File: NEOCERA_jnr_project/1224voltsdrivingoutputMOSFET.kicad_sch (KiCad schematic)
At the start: 15 parts, among them Q1 BSS138, Q2 Q_PMOS_GSD, Q3 BSS138, Q4 Q_PMOS_GSD, Q5 BSS138, Q6 Q_PMOS_GSD

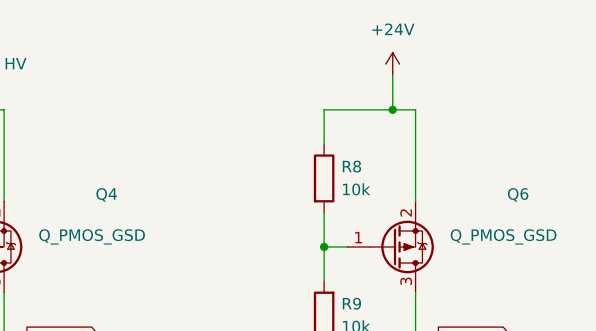
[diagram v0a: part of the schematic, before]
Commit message: changes
edited symbols and usb schematic
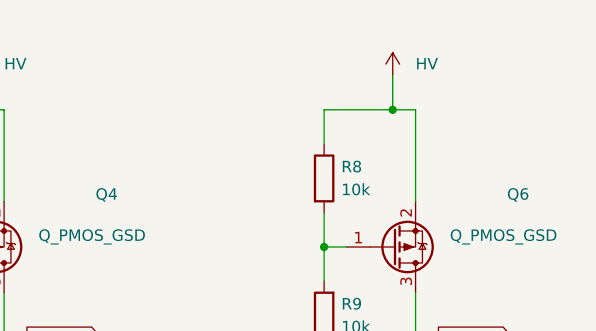
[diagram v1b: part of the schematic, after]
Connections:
- net +24V is gone; now on net HV: Q6.2 (S), R8.1
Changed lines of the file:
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@@
 			)
 		)
-		(property "Value" "+24V"
-			(at 152.4 63.5 0)
+		(property "Value" "HV"
+			(at 154.94 67.3099 0)
 			(effects
 				(font
 					(size 1.27 1.27)
 				)
+				(justify left)
 			)
 		)

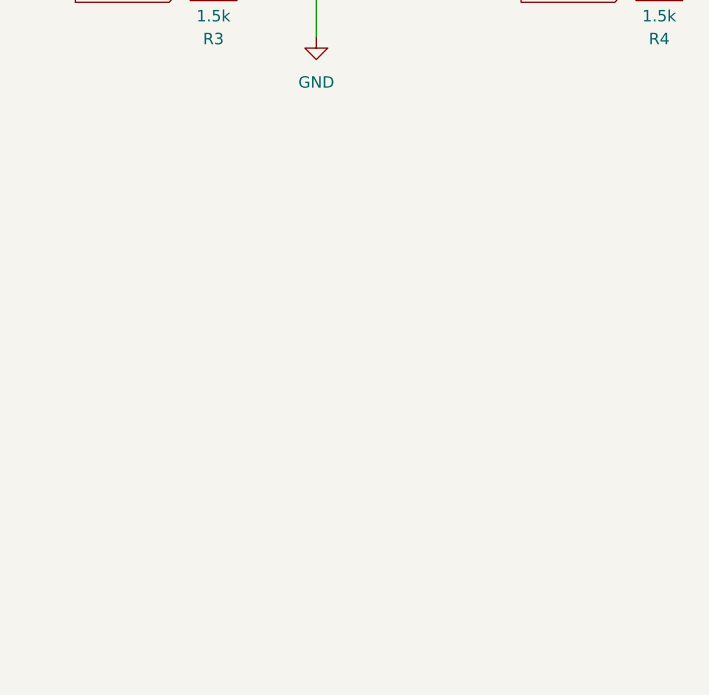
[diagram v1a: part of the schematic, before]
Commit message: updated al the amounts of each item in the schematic
made updates in the amount of each components
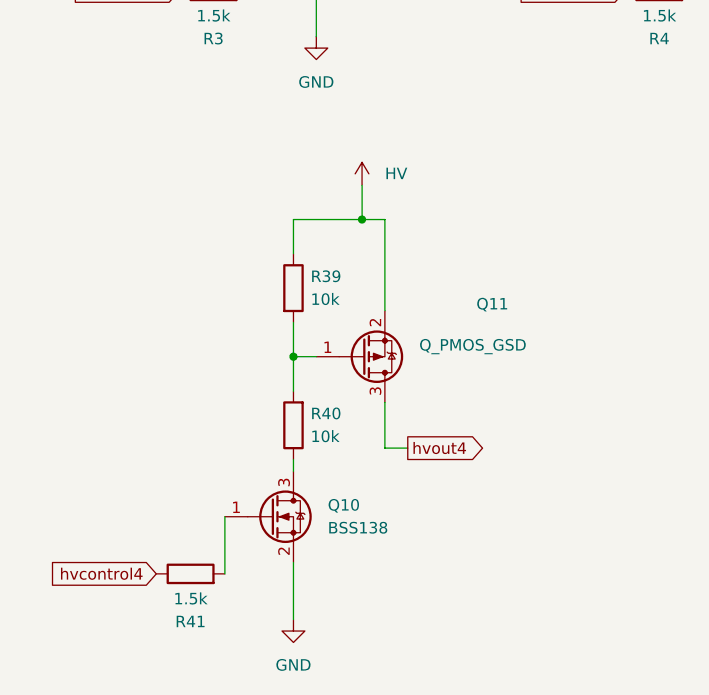
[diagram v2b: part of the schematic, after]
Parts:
- added Q10: BSS138, Package_TO_SOT_SMD:SOT-23_Handsoldering, symbol Transistor_FET:BSS138
- added Q11: Q_PMOS_GSD, Package_TO_SOT_SMD:SOT-23_Handsoldering, symbol Device:Q_PMOS_GSD
- added R39, R40: 10k, Resistor_SMD:R_0603_1608Metric_Pad0.98x0.95mm_HandSolder, symbol Device:R
- added R41: 1.5k, Resistor_SMD:R_0603_1608Metric_Pad0.98x0.95mm_HandSolder, symbol Device:R
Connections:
- net GND: now also Q10.2 (S)
- net HV: now also Q11.2 (S), R39.1
- new net: Q10.3 (D), R40.1
- new net: Q11.1 (G), R39.2, R40.2
- new net: Q10.1 (G), R41.2
- new net hvcontrol4: R41.1
- new net hvout4: Q11.3 (D)

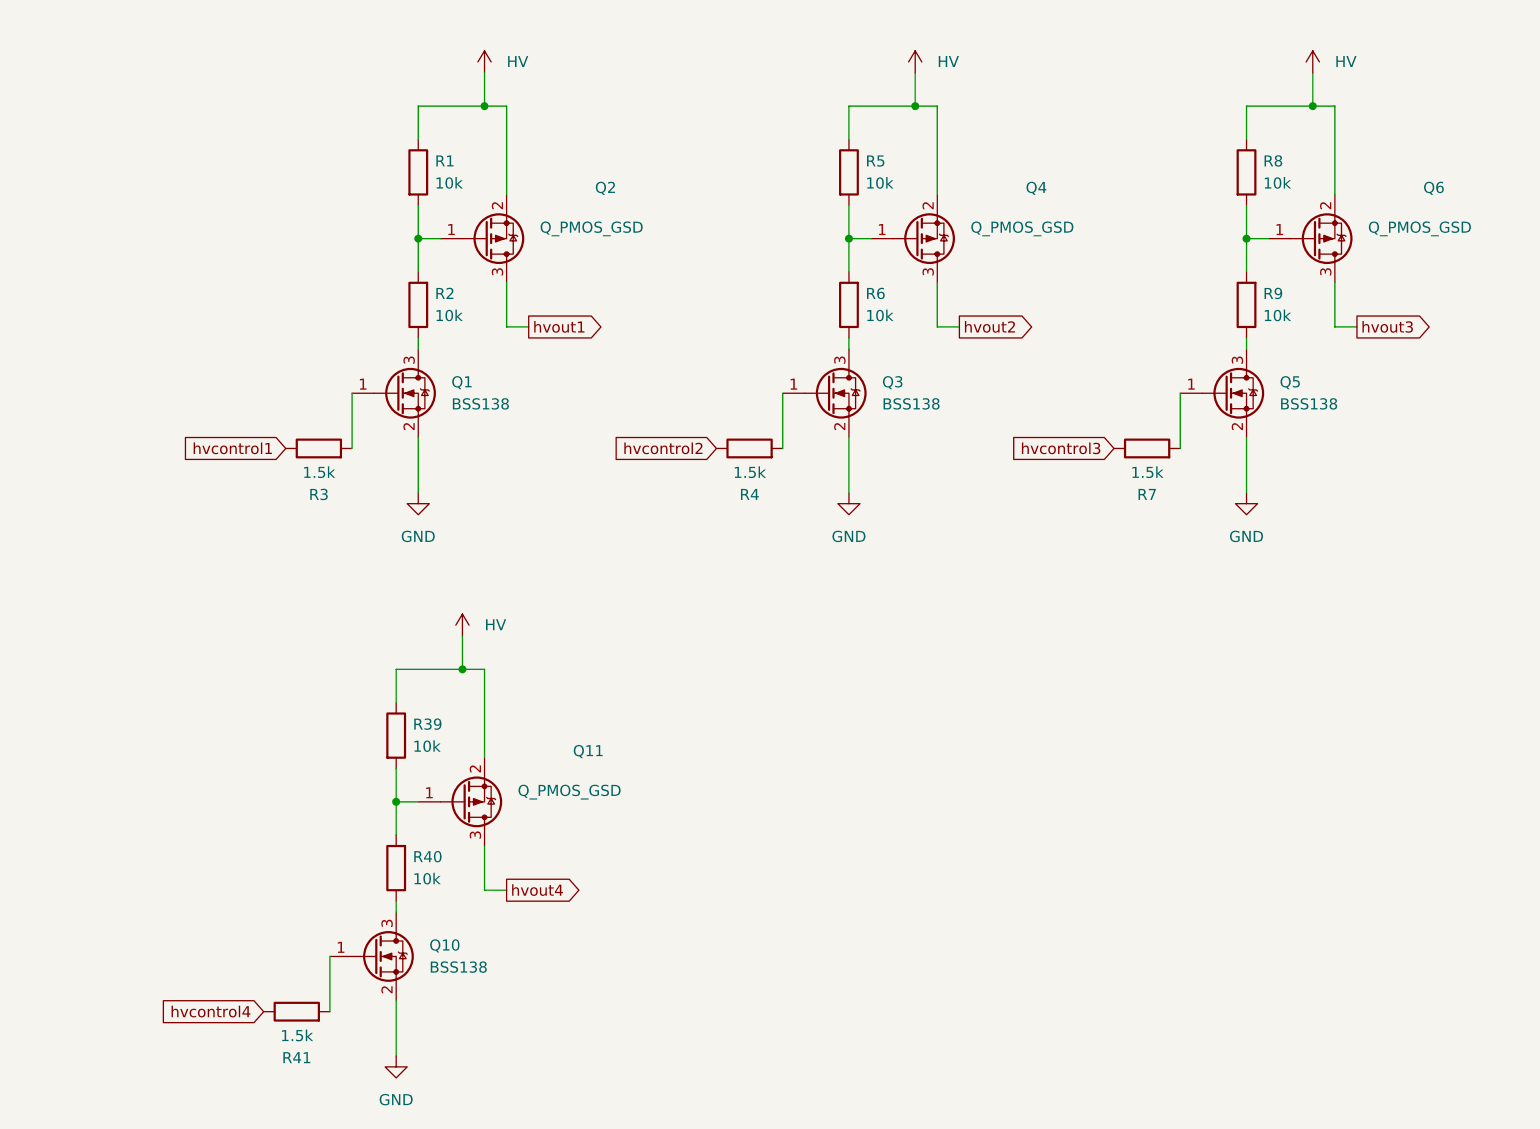
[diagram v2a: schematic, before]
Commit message: Edits made with Dr. Caw.
I added the net to the root
I added the write global nets to some of the previously designed symbols like TX/RX
I added a 3.3V pullup resistor to the opto
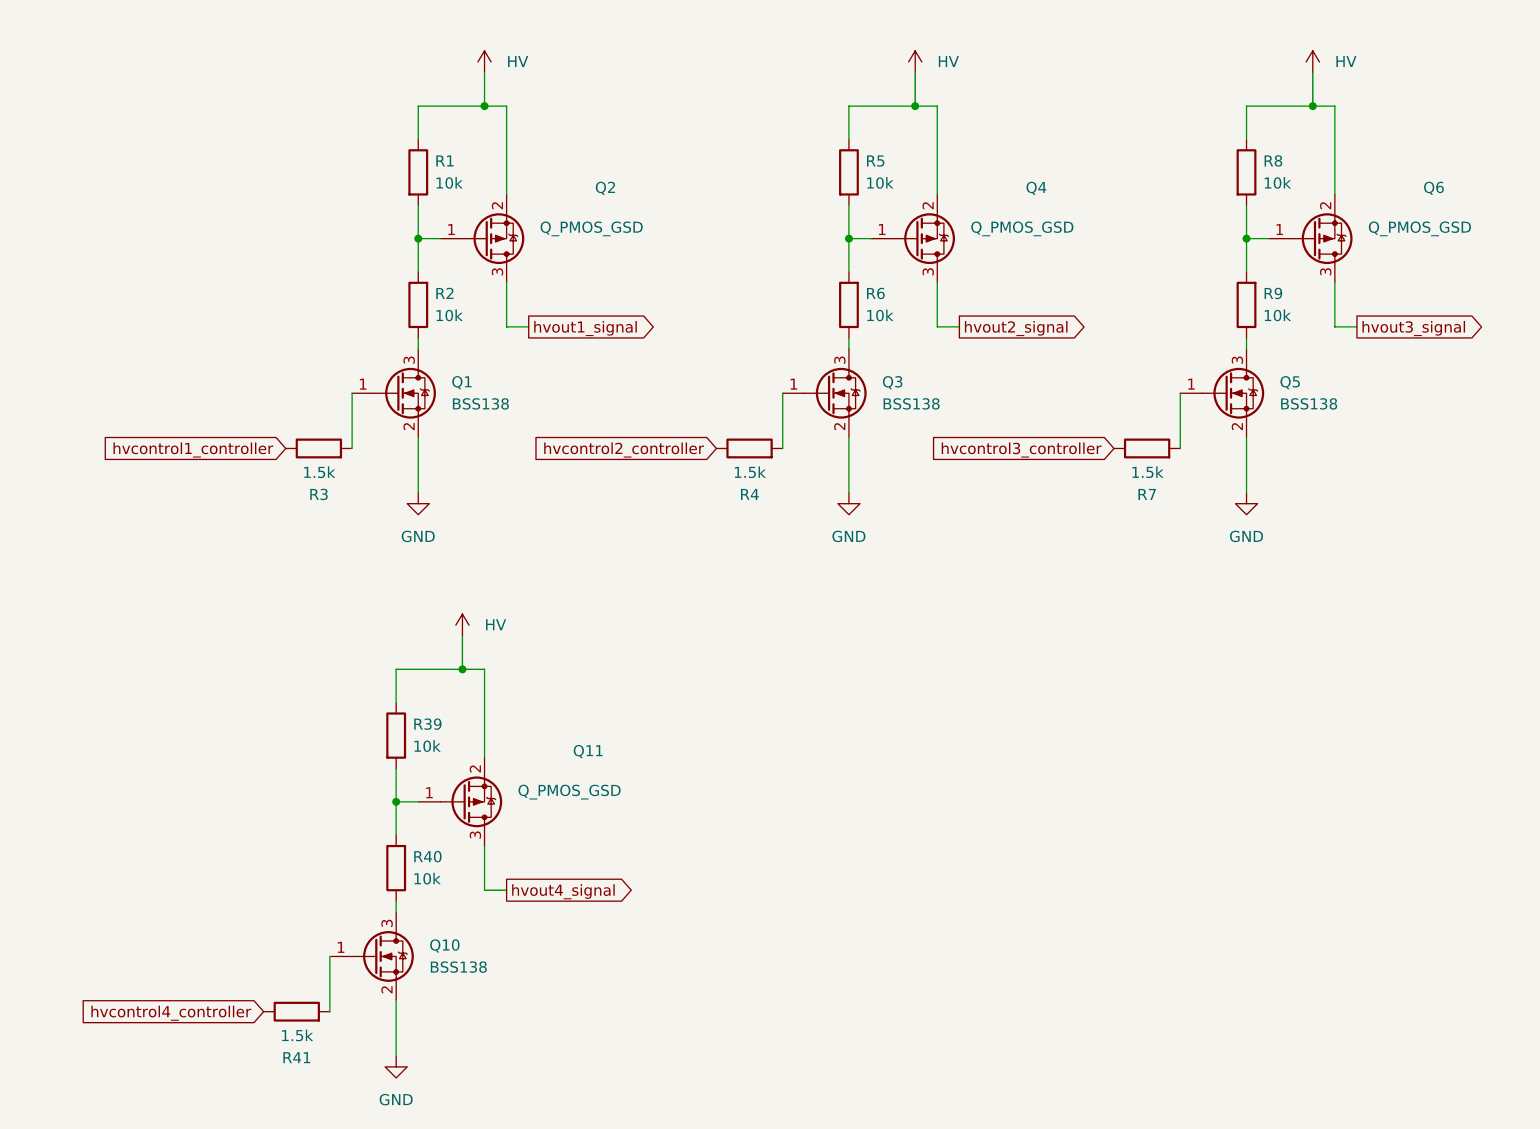
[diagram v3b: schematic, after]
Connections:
- net hvcontrol1 renamed hvcontrol1_controller
- net hvcontrol2 renamed hvcontrol2_controller
- net hvcontrol3 renamed hvcontrol3_controller
- net hvcontrol4 renamed hvcontrol4_controller
- net hvout1 renamed hvout1_signal
- net hvout2 renamed hvout2_signal
- net hvout3 renamed hvout3_signal
- net hvout4 renamed hvout4_signal
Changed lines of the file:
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@@
 		)
 	)
-	(global_label "hvout2"
+	(global_label "hvout2_signal"
 		(shape output)
 		(at 111.76 97.79 0)
@@
 		)
 	)
-	(global_label "hvcontrol3"
+	(global_label "hvcontrol3_controller"
 		(shape input)
 		(at 129.54 111.76 180)
@@
 		)
 	)
-	(global_label "hvcontrol4"
+	(global_label "hvcontrol4_controller"
 		(shape input)
 		(at 31.75 176.53 180)
@@
 		)
 	)
-	(global_label "hvout4"
+	(global_label "hvout4_signal"
 		(shape output)
 		(at 59.69 162.56 0)
@@
 		)
 	)
-	(global_label "hvout3"
+	(global_label "hvout3_signal"
 		(shape output)
 		(at 157.48 97.79 0)
@@
 		)
 	)
-	(global_label "hvout1"
+	(global_label "hvout1_signal"
 		(shape output)
 		(at 62.23 97.79 0)
@@
 		)
 	)
-	(global_label "hvcontrol2"
+	(global_label "hvcontrol2_controller"
 		(shape input)
 		(at 83.82 111.76 180)
@@
 		)
 	)
-	(global_label "hvcontrol1"
+	(global_label "hvcontrol1_controller"
 		(shape input)
 		(at 34.29 111.76 180)
